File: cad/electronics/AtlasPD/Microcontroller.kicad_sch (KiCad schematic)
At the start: 32 parts, among them J1 Conn_02x03_Odd_Even, J201 USB_C_Receptacle_USB2.0, J202 Conn_01x04, SW201 SW_SPST, U201 CP2104, U202 ATmega328P-AU, Y201 CSTNE16M0V53-R0

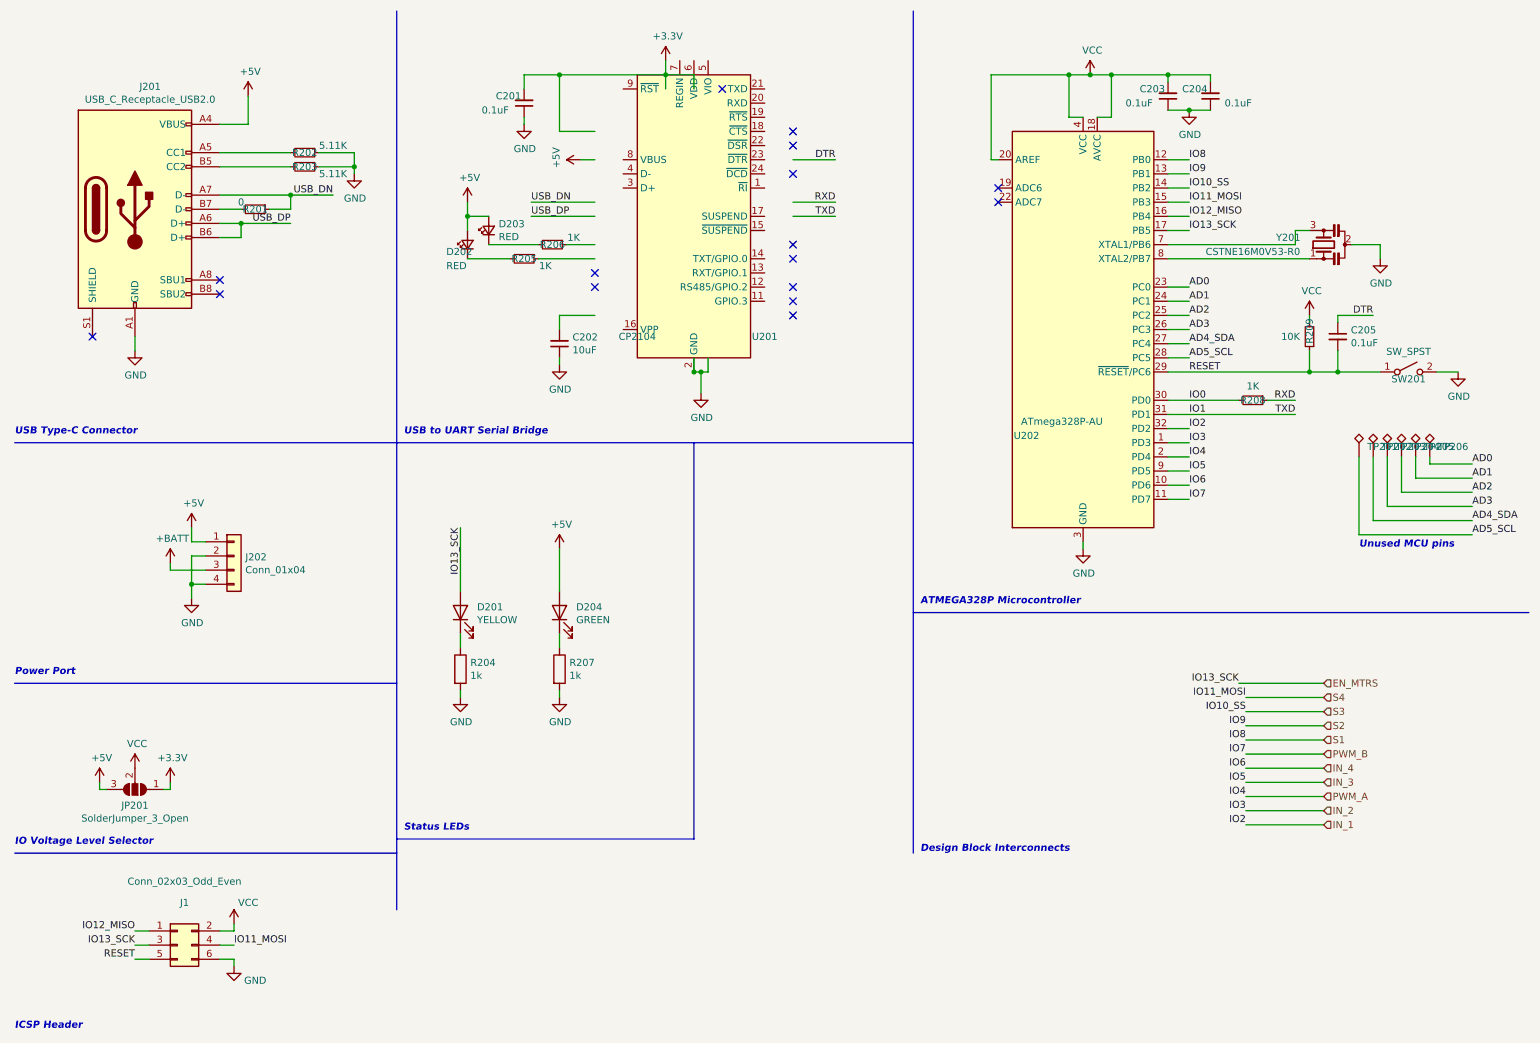
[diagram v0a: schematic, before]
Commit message: Finished IC Schematic, Assigned footprints
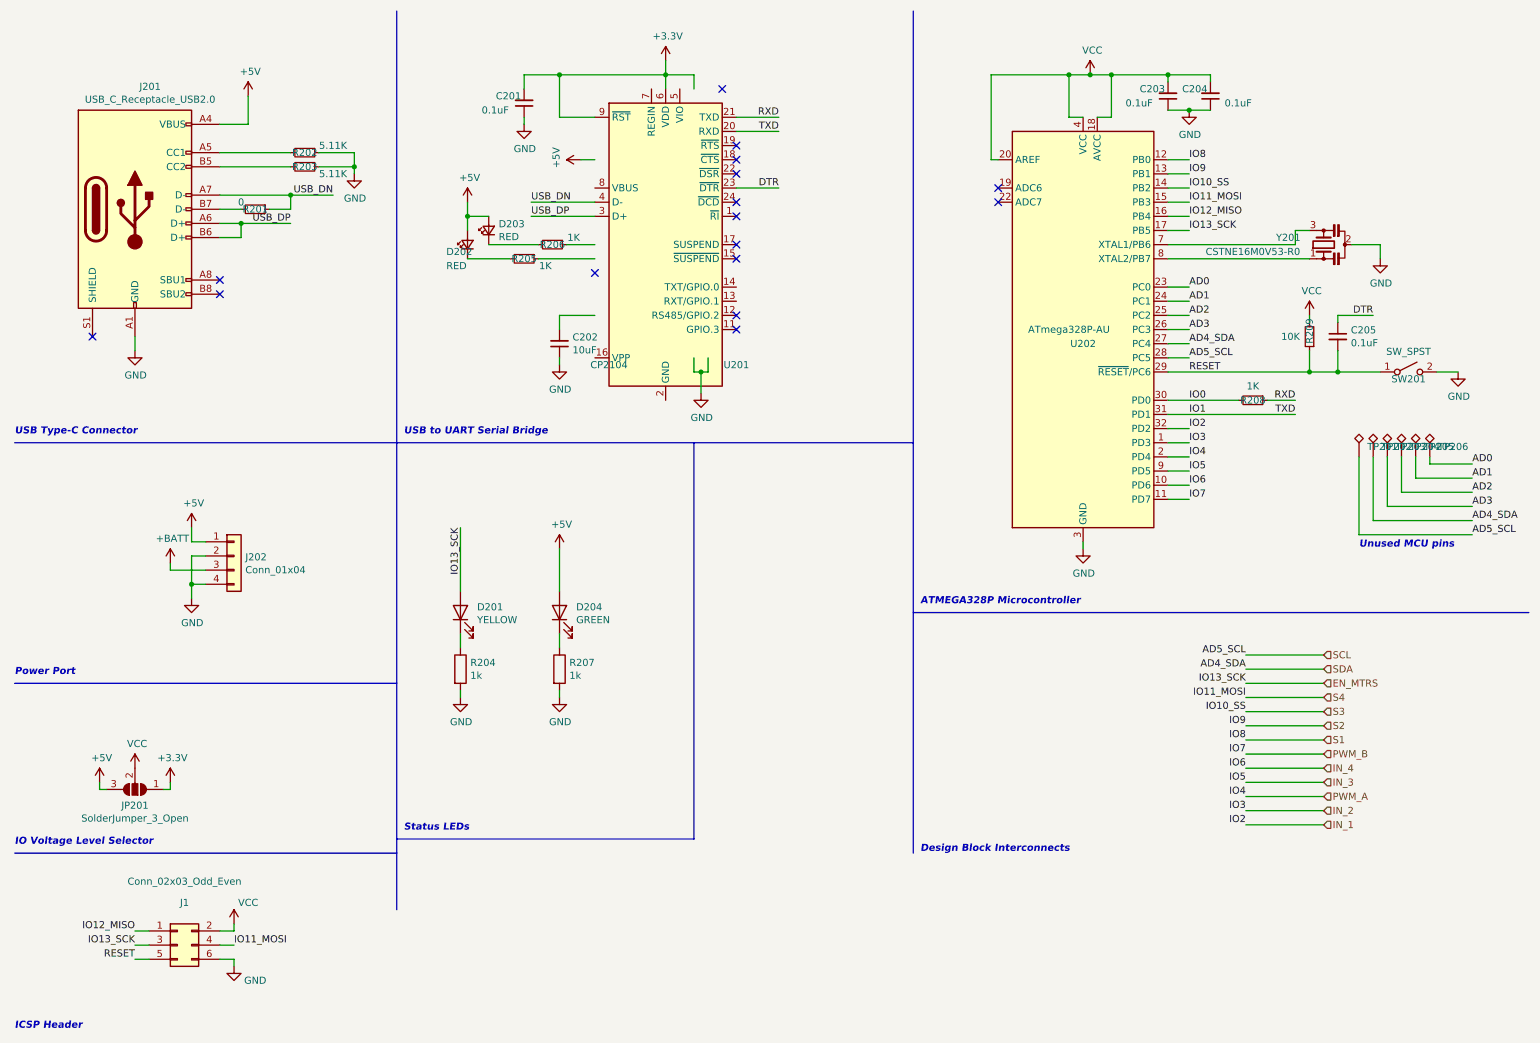
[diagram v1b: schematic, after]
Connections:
- net +3V3: now also U201.6 (VDD), U201.9 (~{RST})
- net DTR: now also U201.23 (~{DTR})
- net GND: no longer U201.2 (GND), U201.25 (GND)
- net IO1: now also U201.20 (RXD)
- net RXD: now also U201.21 (TXD)
- net USB_DN: now also U201.4 (D-)
- net USB_DP: now also U201.3 (D+)
- net AD4_SDA renamed SDA
- net AD5_SCL renamed SCL
- new net: U201.2 (GND), U201.25 (GND)
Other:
- moved on the sheet: U201
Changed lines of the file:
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@@
   (junction (at 110.49 24.13) (diameter 0) (color 0 0 0 0)
   )
-  (junction (at 134.62 77.47) (diameter 0) (color 0 0 0 0)
-  )
   (junction (at 219.71 24.13) (diameter 0) (color 0 0 0 0)
   )
@@
   )
   (no_connect (at 189.23 46.99))
-  (no_connect (at 152.4 67.31))
-  (no_connect (at 116.84 62.23))
+  (no_connect (at 142.24 69.85))
+  (no_connect (at 142.24 46.99))
   (no_connect (at 49.53 63.5))
-  (no_connect (at 152.4 54.61))
+  (no_connect (at 142.24 54.61))
   (no_connect (at 116.84 59.69))
   (no_connect (at 189.23 44.45))
-  (no_connect (at 152.4 64.77))
-  (no_connect (at 152.4 36.83))
-  (no_connect (at 152.4 62.23))
-  (no_connect (at 152.4 57.15))
-  (no_connect (at 152.4 41.91))
+  (no_connect (at 142.24 67.31))
+  (no_connect (at 142.24 39.37))
+  (no_connect (at 142.24 41.91))
+  (no_connect (at 142.24 57.15))
+  (no_connect (at 142.24 49.53))
   (no_connect (at 49.53 60.96))
-  (no_connect (at 152.4 34.29))
+  (no_connect (at 142.24 36.83))
   (no_connect (at 26.67 71.12))
   (no_connect (at 139.7 26.67))
@@
     (stroke (width 0) (type default) (color 0 0 0 0))
   )
-  (wire (pts (xy 152.4 46.99) (xy 160.02 46.99))
+  (wire (pts (xy 142.24 31.75) (xy 149.86 31.75))
     (stroke (width 0) (type default) (color 0 0 0 0))
   )
@@
     (stroke (width 0) (type default) (color 0 0 0 0))
   )
+  (wire (pts (xy 233.68 128.27) (xy 247.65 128.27))
+    (stroke (width 0) (type default) (color 0 0 0 0))
+  )
   (wire (pts (xy 49.53 177.8) (xy 52.07 177.8))
     (stroke (width 0) (type default) (color 0 0 0 0))
@@
     (stroke (width 0) (type default) (color 0 0 0 0))
   )
-  (wire (pts (xy 152.4 39.37) (xy 160.02 39.37))
+  (wire (pts (xy 142.24 44.45) (xy 149.86 44.45))
     (stroke (width 0) (type default) (color 0 0 0 0))
   )
@@
     (stroke (width 0) (type default) (color 0 0 0 0))
   )
-  (wire (pts (xy 232.41 133.35) (xy 247.65 133.35))
-    (stroke (width 0) (type default) (color 0 0 0 0))
-  )
   (wire (pts (xy 245.11 73.66) (xy 245.11 77.47))
     (stroke (width 0) (type default) (color 0 0 0 0))
@@
     (stroke (width 0) (type default) (color 0 0 0 0))
   )
+  (wire (pts (xy 233.68 133.35) (xy 247.65 133.35))
+    (stroke (width 0) (type default) (color 0 0 0 0))
+  )
   (wire (pts (xy 219.71 87.63) (xy 223.52 87.63))
     (stroke (width 0) (type default) (color 0 0 0 0))
@@
     (stroke (width 0) (type default) (color 0 0 0 0))
   )
-  (wire (pts (xy 152.4 49.53) (xy 160.02 49.53))
+  (wire (pts (xy 142.24 34.29) (xy 149.86 34.29))
     (stroke (width 0) (type default) (color 0 0 0 0))
   )
@@
     (stroke (width 0) (type default) (color 0 0 0 0))
   )
+  (wire (pts (xy 110.49 31.75) (xy 110.49 24.13))
+    (stroke (width 0) (type default) (color 0 0 0 0))
+  )
   (wire (pts (xy 44.45 118.11) (xy 44.45 115.57))
     (stroke (width 0) (type default) (color 0 0 0 0))
@@
     (stroke (width 0) (type default) (color 0 0 0 0))
   )
+  (wire (pts (xy 233.68 130.81) (xy 247.65 130.81))
+    (stroke (width 0) (type default) (color 0 0 0 0))
+  )
   (wire (pts (xy 219.71 77.47) (xy 245.11 77.47))
     (stroke (width 0) (type default) (color 0 0 0 0))
@@
     (stroke (width 0) (type default) (color 0 0 0 0))
   )
-  (wire (pts (xy 110.49 34.29) (xy 110.49 24.13))
-    (stroke (width 0) (type default) (color 0 0 0 0))
-  )
   (wire (pts (xy 219.71 54.61) (xy 242.57 54.61))
     (stroke (width 0) (type default) (color 0 0 0 0))
@@
     (stroke (width 0) (type default) (color 0 0 0 0))
   )
-  (wire (pts (xy 116.84 34.29) (xy 110.49 34.29))
+  (wire (pts (xy 116.84 31.75) (xy 110.49 31.75))
     (stroke (width 0) (type default) (color 0 0 0 0))
   )
@@
     (effects (font (size 1.27 1.27)) (justify right bottom))
   )
-  (label "IO13_SCK" (at 232.41 133.35 180)
+  (label "IO13_SCK" (at 233.68 133.35 180)
     (effects (font (size 1.27 1.27)) (justify right bottom))
   )
@@
     (effects (font (size 1.27 1.27)) (justify left bottom))
   )
-  (label "RXD" (at 160.02 46.99 180)
+  (label "RXD" (at 149.86 31.75 180)
     (effects (font (size 1.27 1.27)) (justify right bottom))
   )
@@
     (effects (font (size 1.27 1.27)) (justify right bottom))
   )
-  (label "DTR" (at 160.02 39.37 180)
+  (label "DTR" (at 149.86 44.45 180)
+    (effects (font (size 1.27 1.27)) (justify right bottom))
+  )
+  (label "AD5_SCL" (at 233.68 128.27 180)
     (effects (font (size 1.27 1.27)) (justify right bottom))
   )
@@
     (effects (font (size 1.27 1.27)) (justify right bottom))
   )
-  (label "TXD" (at 160.02 49.53 180)
+  (label "TXD" (at 149.86 34.29 180)
     (effects (font (size 1.27 1.27)) (justify right bottom))
   )
@@
     (effects (font (size 1.27 1.27)) (justify right bottom))
   )
+  (label "AD4_SDA" (at 233.68 130.81 180)
+    (effects (font (size 1.27 1.27)) (justify right bottom))
+  )
   (hierarchical_label "PWM_A" (shape input) (at 247.65 153.67 0)
     (effects (font (size 1.27 1.27)) (justify left))
@@
     (effects (font (size 1.27 1.27)) (justify left))
   )
+  (hierarchical_label "SCL" (shape input) (at 247.65 128.27 0)
+    (effects (font (size 1.27 1.27)) (justify left))
+  )
   (hierarchical_label "PWM_B" (shape input) (at 247.65 146.05 0)
     (effects (font (size 1.27 1.27)) (justify left))
   )
   (hierarchical_label "IN_3" (shape input) (at 247.65 151.13 0)
+    (effects (font (size 1.27 1.27)) (justify left))
+  )
+  (hierarchical_label "SDA" (shape input) (at 247.65 130.81 0)
     (effects (font (size 1.27 1.27)) (justify left))
   )
@@
   (symbol (lib_id "MCU_Microchip_ATmega:ATmega328P-AU") (at 204.47 69.85 0) (unit 1)
     (in_bom yes) (on_board yes)
-    (property "Reference" "U202" (id 0) (at 194.31 88.9 0))
-    (property "Value" "ATmega328P-AU" (id 1) (at 200.66 86.36 0))
+    (property "Reference" "U202" (id 0) (at 204.47 72.39 0))
+    (property "Value" "ATmega328P-AU" (id 1) (at 201.93 69.85 0))
     (property "Footprint" "Package_QFP:TQFP-32_7x7mm_P0.8mm" (id 2) (at 204.47 69.85 0)
       (effects (font (size 1.27 1.27) italic) hide)
@@
     (pin "1")
   )
-  (symbol (lib_id "Interface_USB:CP2104") (at 134.62 49.53 0) (unit 1)
+  (symbol (lib_id "Interface_USB:CP2104") (at 129.54 54.61 0) (unit 1)
     (in_bom yes) (on_board yes)
-    (property "Reference" "U201" (id 0) (at 147.32 71.12 0))
-    (property "Value" "CP2104" (id 1) (at 124.46 71.12 0))
-    (property "Footprint" "Package_DFN_QFN:QFN-24-1EP_4x4mm_P0.5mm_EP2.6x2.6mm" (id 2) (at 138.43 73.66 0)
+    (property "Reference" "U201" (id 0) (at 142.24 76.2 0))
+    (property "Value" "CP2104" (id 1) (at 119.38 76.2 0))
+    (property "Footprint" "Package_DFN_QFN:QFN-24-1EP_4x4mm_P0.5mm_EP2.6x2.6mm" (id 2) (at 133.35 78.74 0)
       (effects (font (size 1.27 1.27)) (justify left) hide)
     )
-    (property "Datasheet" "https://www.silabs.com/documents/public/data-sheets/cp2104.pdf" (id 3) (at 120.65 17.78 0)
-      (effects (font (size 1.27 1.27)) hide)
-    )
-    (property "LCSC Part #" "C47742" (id 4) (at 134.62 49.53 0)
-      (effects (font (size 1.27 1.27)) hide)
-    )
-    (property "LCSC" "C47742" (id 5) (at 134.62 49.53 0)
-      (effects (font (size 1.27 1.27)) hide)
-    )
+    (property "Datasheet" "https://www.silabs.com/documents/public/data-sheets/cp2104.pdf" (id 3) (at 115.57 22.86 0)
+      (effects (font (size 1.27 1.27)) hide)
+    )
+    (property "LCSC Part #" "C47742" (id 4) (at 129.54 54.61 0)
+      (effects (font (size 1.27 1.27)) hide)
+    )
+    (property "LCSC" "C47742" (id 5) (at 129.54 54.61 0)
+      (effects (font (size 1.27 1.27)) hide)
+    )

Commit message: Fixed schematic issues from KiCAD upgrade, Moved 3.3V LDO to MCU Sheet
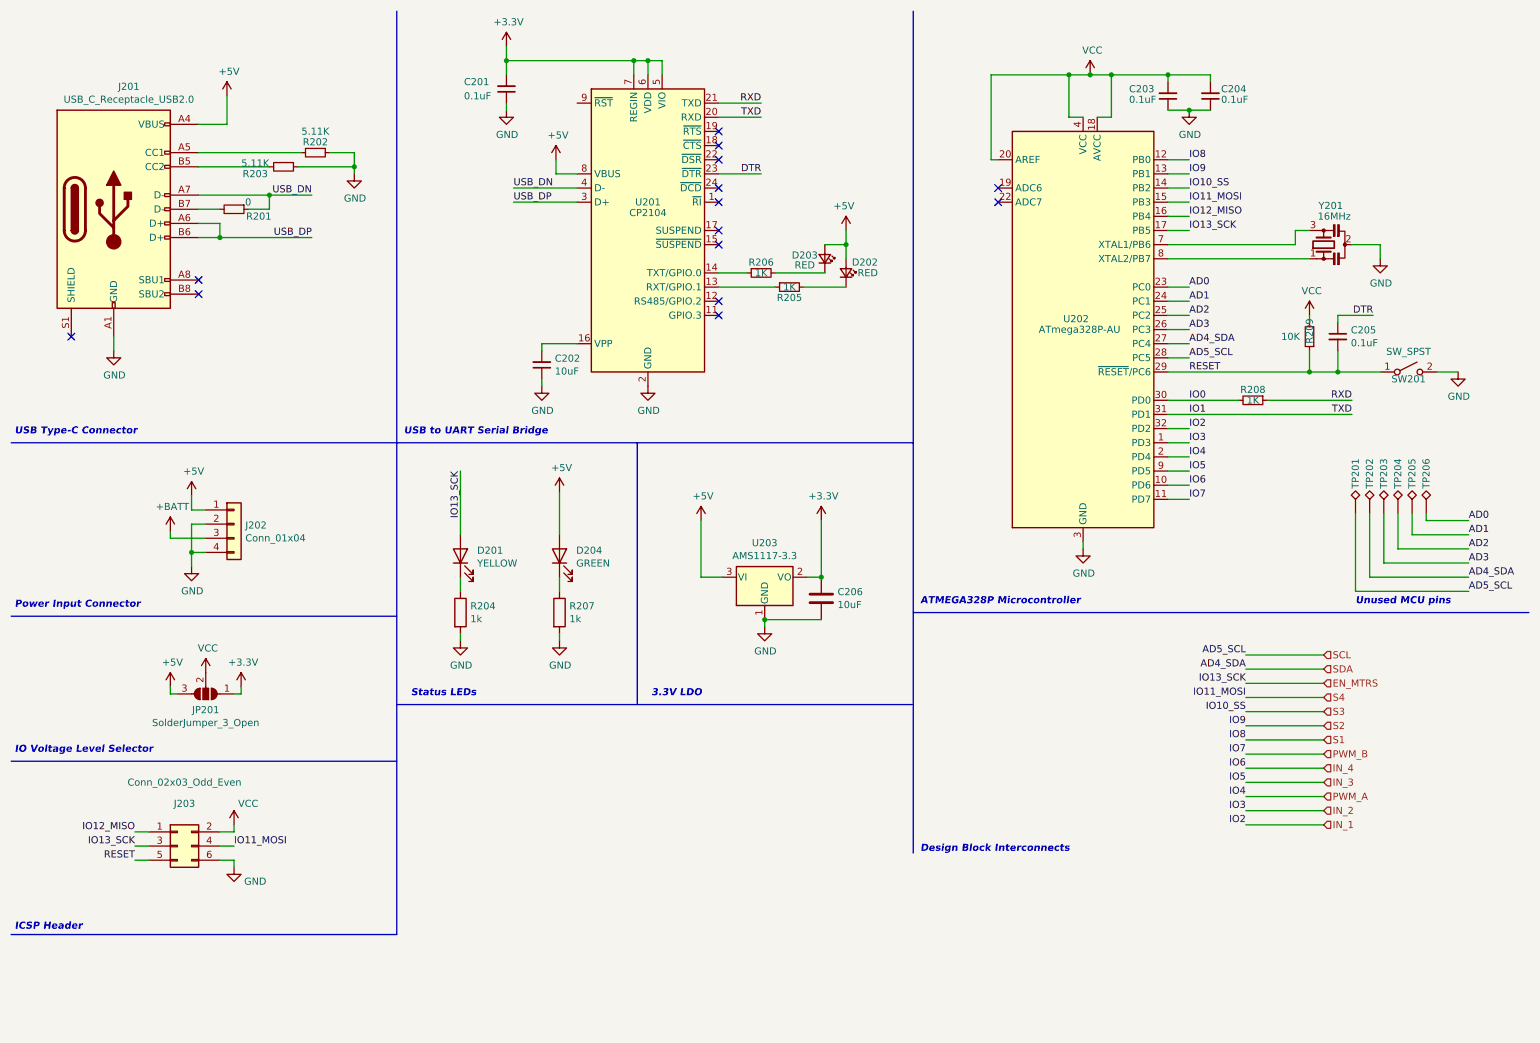
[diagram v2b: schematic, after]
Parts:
- added C206: 10uF, Capacitor_SMD:C_0603_1608Metric, symbol Device:C
- added U203: AMS1117-3.3, Package_TO_SOT_SMD:SOT-223-3_TabPin2, symbol Regulator_Linear:AMS1117-3.3
- Y201: value CSTNE16M0V53-R0 -> 16MHz; LCSC C341521 -> (none); LCSC Part # C341521 -> (none); Model (none) -> CSTNE16M0V53-R0
- renumbered J1 to J203
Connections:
- net +3V3: now also U201.5 (VIO), U201.7 (REGIN), C206.1, U203.2 (VO); no longer U201.9 (~{RST})
- net +5V: now also U201.8 (VBUS), U203.3 (VI)
- net GND: now also U201.2 (GND), U201.25 (GND), C206.2, U203.1 (GND)
- net at U201.13 (RXT/GPIO.1): now also R205.1
- net at U201.14 (TXT/GPIO.0): now also R206.1
- net at U201.16 (VPP): now also C202.2
- no-connect marks 16 -> 14
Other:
- note added: "3.3V LDO"
- note added: "Power Input Connector"
- note removed: "Power Port"
- moved on the sheet: C201, C202, D201, D202, D203, D204, J201, J202, J203, JP201, R201, R202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
